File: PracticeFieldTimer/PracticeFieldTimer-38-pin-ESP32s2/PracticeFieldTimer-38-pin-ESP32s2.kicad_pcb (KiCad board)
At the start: 2 copper layers, 23 parts, among them J1 External Controls, J2 4 x 20 I2C LCD, J3 Panel, J4 DS3231 Module, J5 /CAN Enable, J6 RJ45, J7 RJ45, J8 CAN Terminate, U1 ESP32-DevKitC, U2 SN65HVD230DR

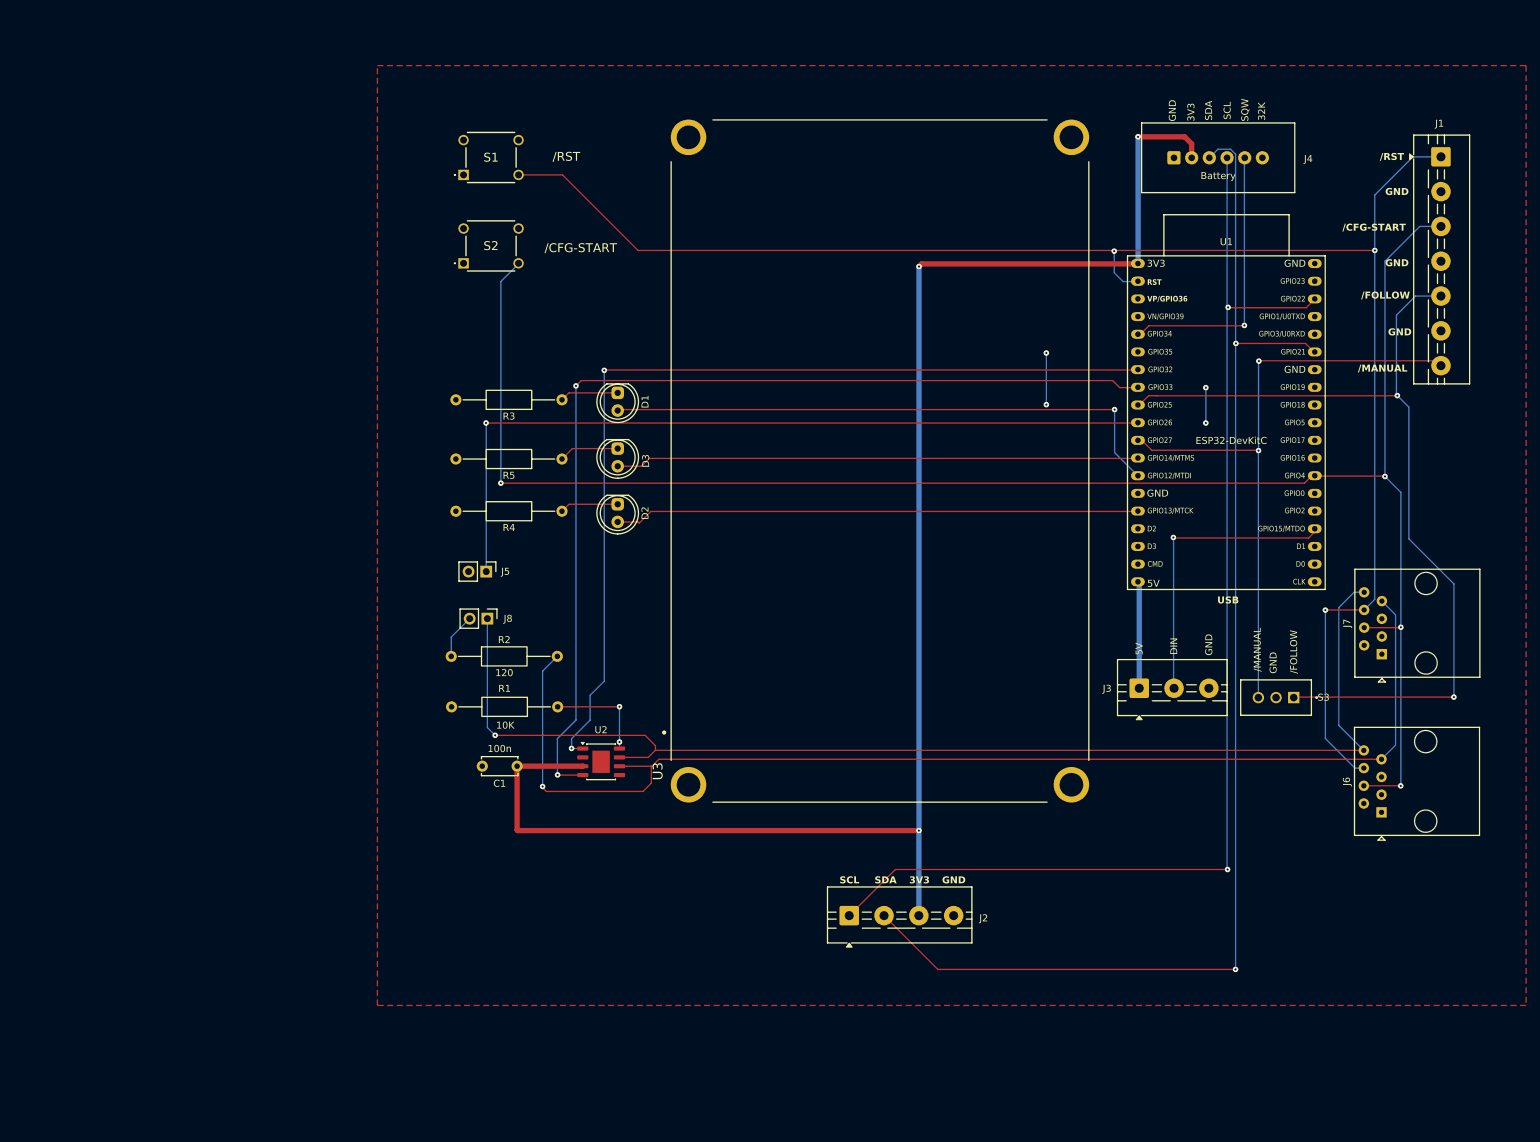
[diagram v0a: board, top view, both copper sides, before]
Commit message: Fix LCD header, which was wired backwards.
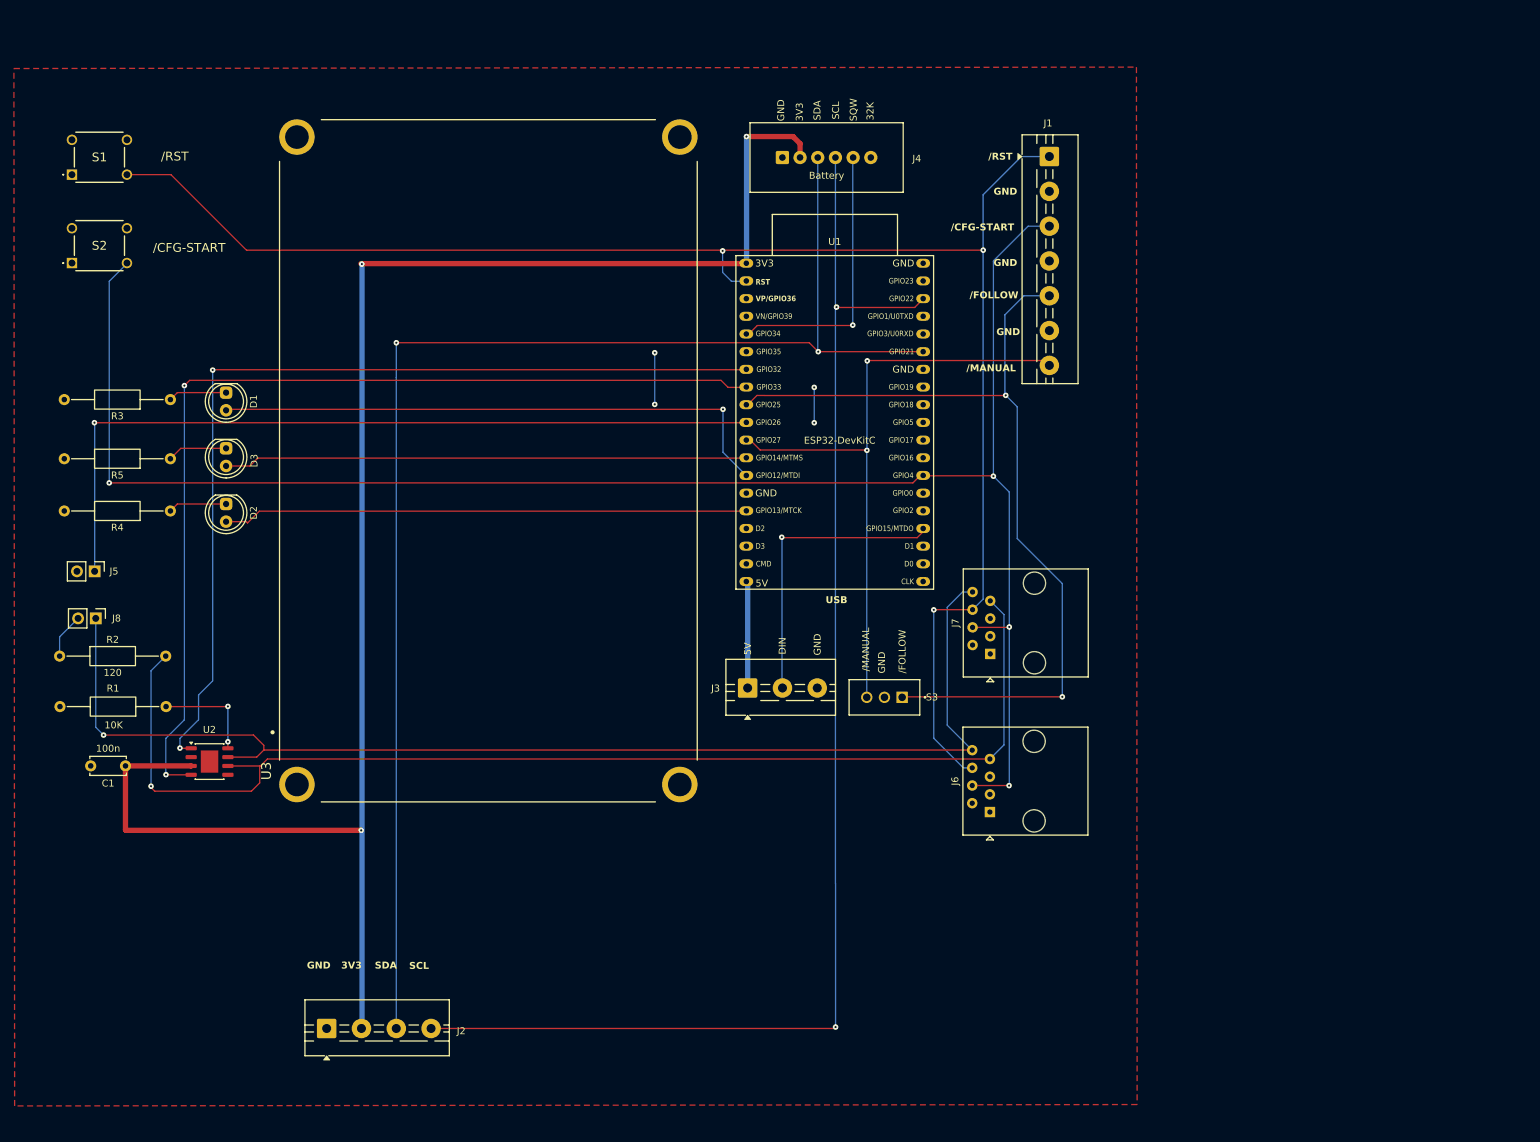
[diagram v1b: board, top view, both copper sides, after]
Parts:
- moved J2 76.8 mm to (59.4, 165.7)
- moved J1 56.3 mm to (163.2, 40.5)
- moved J4 56.3 mm to (131.2, 40.6)
- moved J6 56.3 mm to (154.7, 134.6)
- moved S3 56.3 mm to (139.6, 118.1)
- moved U1 56.3 mm to (119.7, 55.8)
- moved C1 56.3 mm to (30.5, 128.0)
- moved R1 56.3 mm to (36.4, 119.5)
- moved J3 56.3 mm to (119.9, 116.8)
- moved J5 56.3 mm to (26.1, 100.0)
- moved J8 56.3 mm to (26.3, 106.8)
- moved R2 56.3 mm to (21.1, 112.2)
- moved S1 56.3 mm to (22.8, 43.1)
- moved S2 56.3 mm to (22.8, 55.8)
- moved U2 56.3 mm to (42.6, 127.4)
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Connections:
- J2 pad 1: I2C SCL -> GND
- J2 pad 2: I2C SDA -> +3.3V
- J2 pad 3: +3.3V -> I2C SDA
- J2 pad 4: GND -> I2C SCL
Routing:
- net I2C SCL: track 172.0 -> 196.0 mm
- net +3.3V: track 229.6 -> 246.2 mm
- net I2C SDA: track 187.4 -> 202.6 mm

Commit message: Adjust part placement and routing. Annotate the board with copyright &c. Set the edges. Next step: mounting holes.
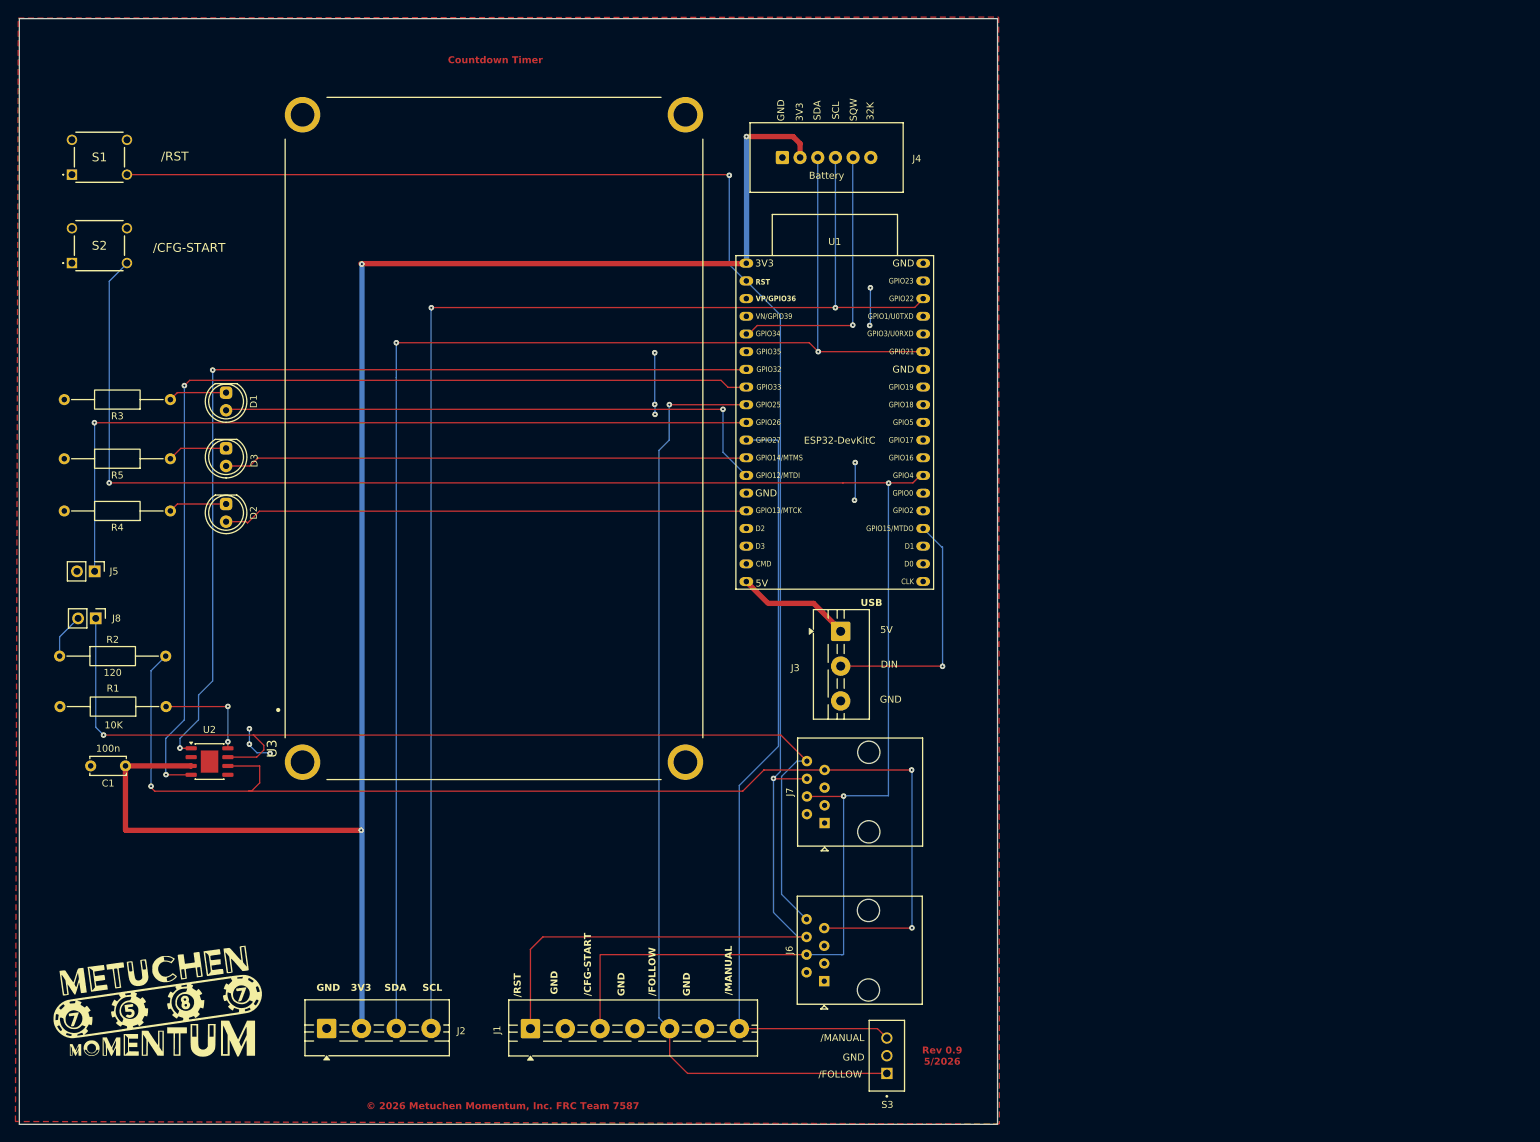
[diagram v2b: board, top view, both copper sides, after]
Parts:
- added G***: LOGO, Misc:MetuchenMomentumLogo, F.Cu at (35.2, 161.8)
- moved J1 145.8 mm to (88.7, 165.7), turned to 0 degrees
- moved S3 51.5 mm to (139.9, 169.6), turned to 90 degrees
- moved J7 34.0 mm to (131.0, 136.2)
- moved J6 34.0 mm to (130.9, 158.9)
- moved J3 15.6 mm to (133.3, 108.7), turned to -90 degrees
- moved U3 3.30 mm to (83.5, 81.0)
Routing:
- net /RST: track 238.5 -> 259.4 mm, vias 3 -> 2
- net CANH: track 175.4 -> 154.7 mm
- net /Manual: track 94.3 -> 113.1 mm, vias 2 -> 0
- net /CFG-START: track 256.3 -> 274.8 mm, vias 4 -> 3
- net GND: track 12.3 -> 25.5 mm, vias 4 -> 10
- net /Follow: track 126.5 -> 138.0 mm, vias 2 -> 1
- net Panel DOUT: track 43.9 -> 35.5 mm
- net CANL: track 172.6 -> 174.8 mm, vias 1 -> 3
- net +5V: track 15.3 -> 16.7 mm
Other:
- board outline added: 140.5 x 158.8 mm
- board text added: "Countdown Timer"
- board text added: "Rev 0.9 5/2026"
- board text added: "© 2026 Metuchen Momentum, Inc. FRC Team 7587"

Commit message: Add mounting holes. Note that the LCD Module mounting holes will do double duty. Label more parts and clean up a bit more.
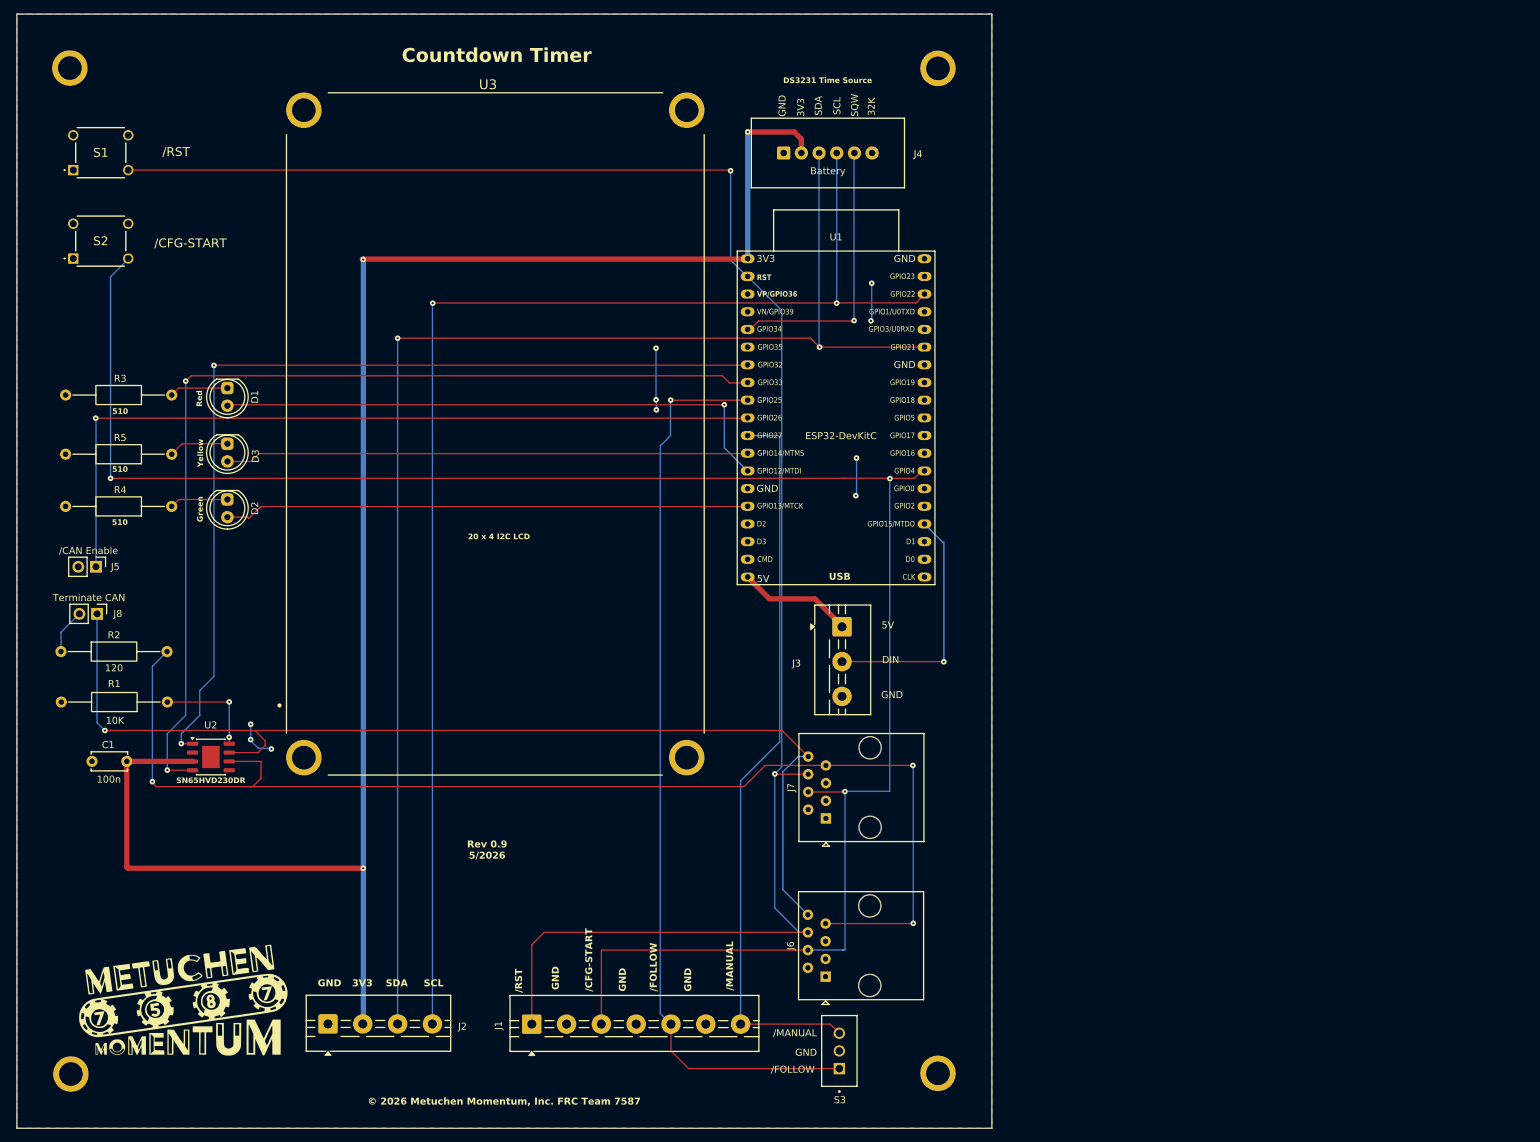
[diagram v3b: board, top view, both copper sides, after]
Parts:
- added ?: , , F.Cu at (22.6, 27.8)
- added ?: , , F.Cu at (22.7, 172.2)
- added ?: , , F.Cu at (147.2, 172.2)
- added ?: , , F.Cu at (147.2, 27.8)
- moved S3 6.86 mm to (133.1, 168.9)
- moved G*** 3.68 mm to (38.8, 161.7)
- moved J1 0.68 mm to (88.9, 165.1)
- moved J4 0.68 mm to (131.4, 39.9)
- moved R1 0.68 mm to (36.6, 118.8)
- moved S1 0.68 mm to (23.0, 42.4)
- moved S2 0.68 mm to (23.0, 55.1)
- moved U2 0.68 mm to (42.8, 126.7)
- moved U3 0.68 mm to (83.7, 80.3)
- moved C1 0.68 mm to (30.7, 127.3)
- moved J5 0.68 mm to (26.3, 99.4)
- moved J8 0.68 mm to (26.5, 106.1)
- moved R2 0.68 mm to (21.3, 111.6)
- moved U1 0.68 mm to (119.9, 55.1)
- moved J2 0.68 mm to (59.6, 165.1)
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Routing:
- net /Follow: track 138.0 -> 131.0 mm
- net /Manual: track 113.1 -> 106.1 mm
- net +3.3V: track 246.2 -> 252.3 mm
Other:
- board size 140.5 x 158.8 mm -> 140.1 x 160 mm
- board text added: "/CAN Enable"
- board text added: "20 x 4 I2C LCD"
- board text added: "510"
- board text added: "DS3231 Time Source"
- board text added: "Green"
- board text added: "Red"
- board text added: "SN65HVD230DR"
- board text added: "Terminate CAN"
- board text added: "Yellow"

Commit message: Move traces away from the RJ-45 jacks, which appear to have metal jackets. Add detail to annotations, correct typoz, adjust fonts.
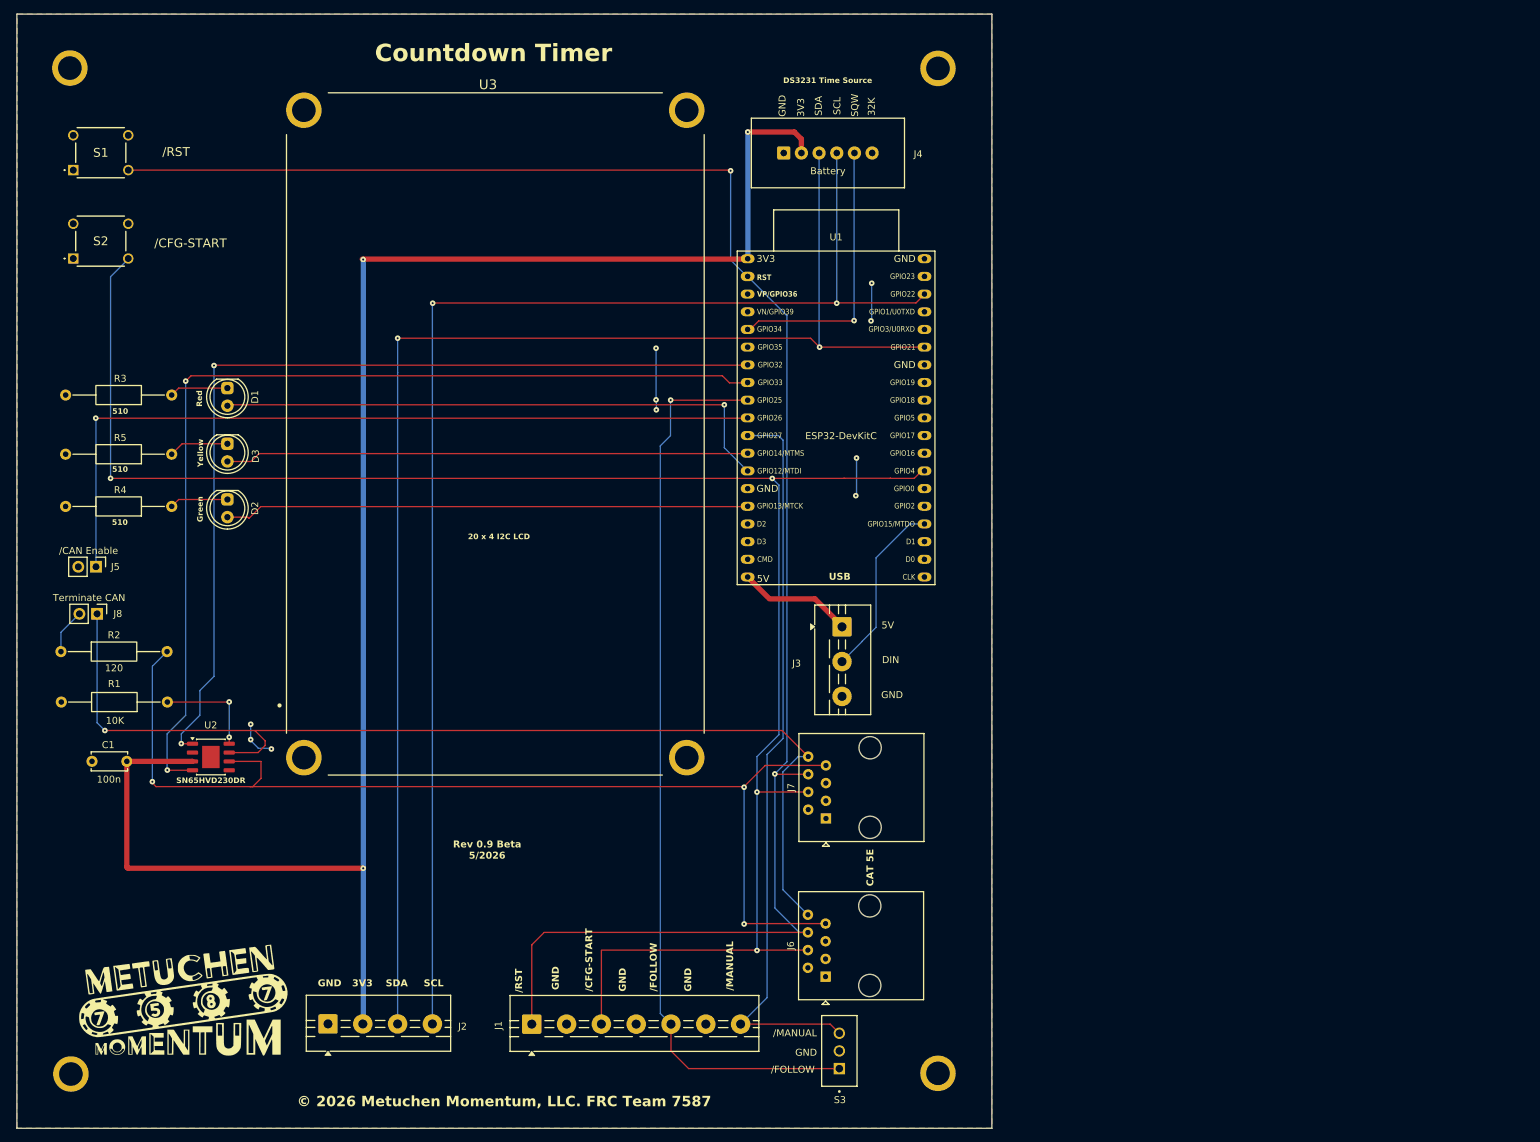
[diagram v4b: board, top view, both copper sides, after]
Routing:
- net CANL: track 174.8 -> 158.3 mm
- net Panel DOUT: track 35.5 -> 25.9 mm, vias 1 -> 0
- net /CFG-START: track 274.8 -> 266.7 mm, vias 3 -> 4
- net /RST: track 259.4 -> 260.1 mm
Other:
- board text added: "CAT 5E"
- board text added: "Rev 0.9 Beta 5/2026"
- board text added: "© 2026 Metuchen Momentum, LLC. FRC Team 7587"
- board text removed: "Rev 0.9 5/2026"
- board text removed: "© 2026 Metuchen Momentum, Inc. FRC Team 7587"
